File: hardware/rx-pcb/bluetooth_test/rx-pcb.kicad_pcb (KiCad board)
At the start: 4 copper layers, 23.1 x 37.6 mm, 33 parts, among them J1 Conn_01x05_Pin, J2 Conn_01x04_Pin, J3 Conn_Coaxial_Small, J4 Conn_01x04_Pin, J5 Conn_01x02_Pin, SW1 SW_SPST, U1 STM32WB05KZV6TR, U2 STS4L-AD1B-R3, U3 LMT70AYFQR, X1 Q22FA12800025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

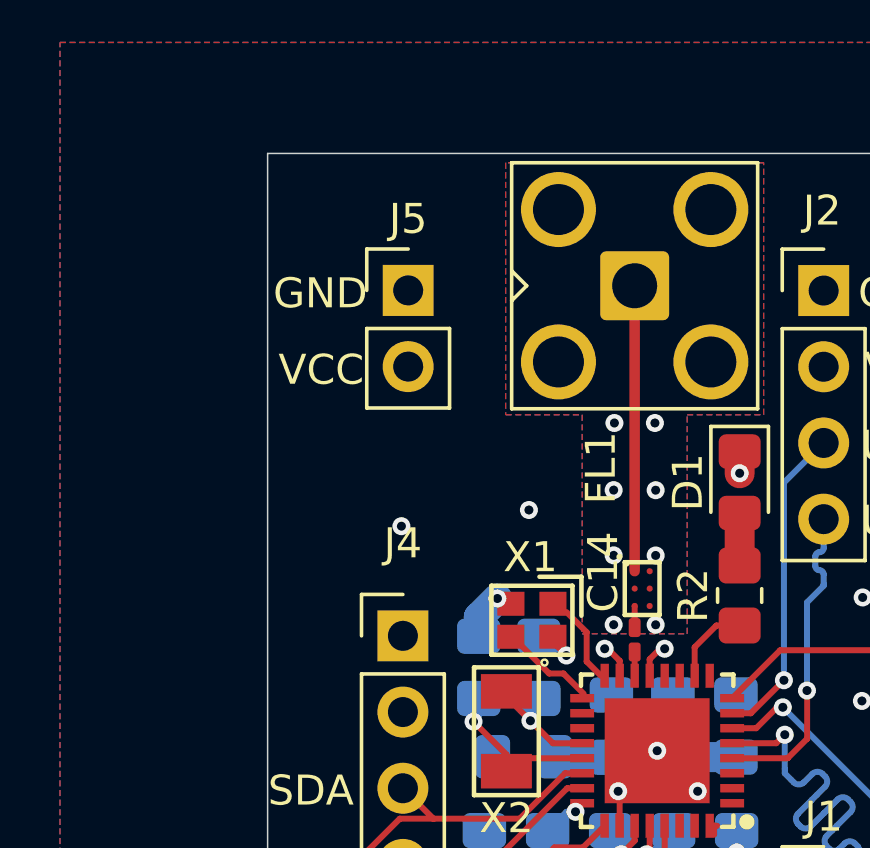
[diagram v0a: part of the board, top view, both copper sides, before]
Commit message: fixed pwr header silkscreen mismatch. added reverse bias protection diode. added power good indicator diode for testing (DNP on final iteration)
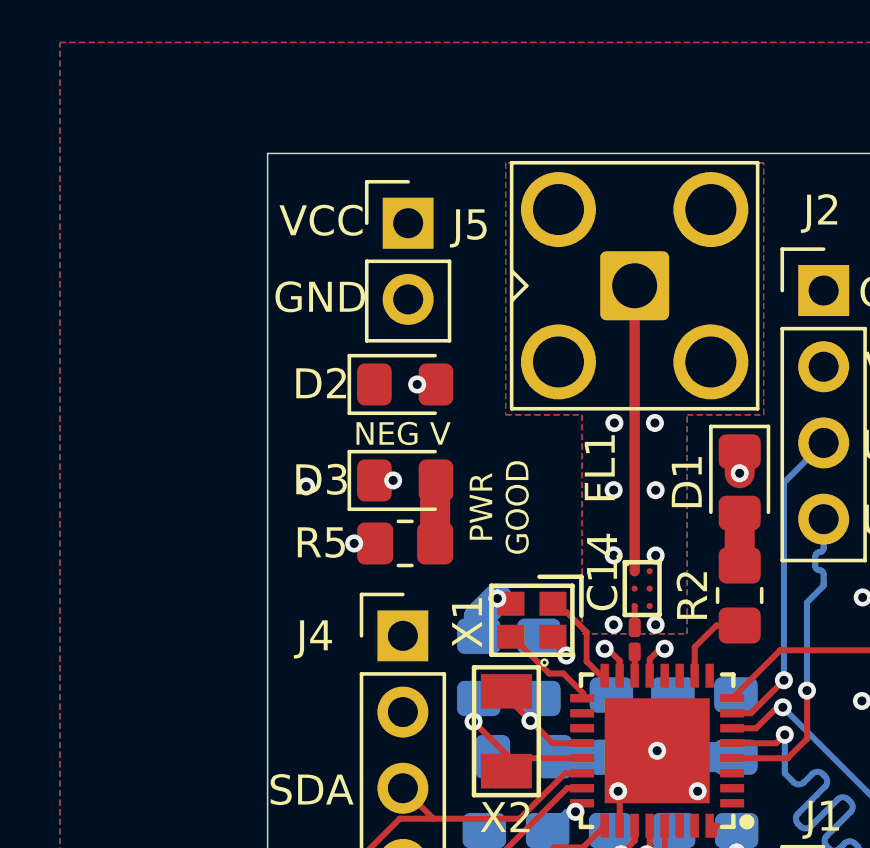
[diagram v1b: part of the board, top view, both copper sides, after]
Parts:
- added D2: LED, rx-parts:LED_0805_2012Metric_Pad1.15x1.40mm_HandSolder, F.Cu at (146.8, 89.4)
- added D3: LED, rx-parts:LED_0805_2012Metric_Pad1.15x1.40mm_HandSolder, F.Cu at (146.8, 92.6)
- added R5: 10k, rx-parts:R_0805_2012Metric_Pad1.20x1.40mm_HandSolder, F.Cu at (146.8, 94.7)
- moved J5 2.24 mm to (146.9, 84.0)
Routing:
- net Net-(D3-A): track 0.00 -> 2.11 mm
- net VCC: vias 12 -> 13
- net GND: vias 22 -> 23
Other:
- board text added: "NEG V"
- board text added: "PWR GOOD"
